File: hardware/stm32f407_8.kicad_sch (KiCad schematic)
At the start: 28 parts, among them J10 Conn_01x04, J8 USB_B_Mini, J9 Conn_01x04, SW3 SW TACT-SPST, U7 STM32F407VGT6, Y3 ABM8G-8.000MHZ-18-D2Y-T

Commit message: Complete Schematic for Power Section
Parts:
- renumbered C70 to C54, C66 to C55, C67 to C56, C62 to C57, C68 to C58, C63 to C59, C64 to C60, C71 to C61, C61 to C62, C65 to C63, C60 to C64, C59 to C65, C55 to C66, C56 to C67, C57 to C68, C58 to C69, C69 to C70, C72 to C71, R28 to R23, R23 to R25

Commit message: Organize schematic
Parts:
- J8: value USB_B_Mini -> GMSB0531112YEU
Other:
- note added: "C54 must be placed close to 1 VDD pin"
- note added: "Main Controller"
- note added: "Oscilator"
- note added: "UART & CAN"
- note added: "USB Mini B"
- note removed: "Must be placed close to 1 VDD pin"
- moved on the sheet: C54, C55, C56, C57, C58, C59, C60, C61, C62, C63, C64, C65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

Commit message: Link footprints to Symbols
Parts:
- C54, C55, C56, C57, C58, C59, C60, C61, C62, C63, C64, C65, C66, C67, C68, C69, C70, C71: footprint (none) -> STM32F407 Dev Kit Library:C_0805_2012Metric_Pad1.18x1.45mm_HandSolder
- FB4: footprint Package_DFN_QFN:QFN-16-1EP_4x4mm_P0.65mm_EP2.1x2.1mm -> STM32F407 Dev Kit Library:C_0805_2012Metric_Pad1.18x1.45mm_HandSolder
- J10, J9: footprint Package_QFP:LQFP-48_7x7mm_P0.5mm -> STM32F407 Dev Kit Library:PinHeader_1x04_P2.54mm_Vertical
- J8: footprint RF_Module:ST-SiP-LGA-86-11x7.3mm -> STM32F407 Dev Kit Library:USB_Mini-B_Wuerth_65100516121_Horizontal
- R23: footprint Package_QFP:LQFP-100_14x14mm_P0.5mm -> STM32F407 Dev Kit Library:R_0805_2012Metric_Pad1.20x1.40mm_HandSolder
- R24, R25: footprint (none) -> STM32F407 Dev Kit Library:R_0805_2012Metric_Pad1.20x1.40mm_HandSolder
- SW3: footprint Button_Switch_SMD:Nidec_Copal_CAS-120A -> STM32F407 Dev Kit Library:SW_Push_1P1T_NO_CK_KSC9xxG
- U7: footprint Package_QFP:LQFP-100_14x14mm_P0.5mm -> STM32F407 Dev Kit Library:LQFP-100_14x14mm_P0.5mm
- Y3: footprint (none) -> STM32F407 Dev Kit Library:Crystal_SMD_3225-4Pin_3.2x2.5mm_HandSoldering
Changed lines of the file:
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@@
 			)
 		)
-		(property "Footprint" "Package_QFP:LQFP-100_14x14mm_P0.5mm"
+		(property "Footprint" "STM32F407 Dev Kit Library:R_0805_2012Metric_Pad1.20x1.40mm_HandSolder"
 			(at 56.642 59.69 90)
 			(hide yes)
@@
 			)
 		)
-		(property "Footprint" ""
+		(property "Footprint" "STM32F407 Dev Kit Library:R_0805_2012Metric_Pad1.20x1.40mm_HandSolder"
 			(at 156.972 104.14 90)
 			(hide yes)
@@
 			)
 		)
-		(property "Footprint" ""
+		(property "Footprint" "STM32F407 Dev Kit Library:C_0805_2012Metric_Pad1.18x1.45mm_HandSolder"
 			(at 196.5452 156.21 0)
 			(hide yes)
@@
 			)
 		)
-		(property "Footprint" ""
+		(property "Footprint" "STM32F407 Dev Kit Library:C_0805_2012Metric_Pad1.18x1.45mm_HandSolder"
 			(at 166.0652 40.64 0)
 			(hide yes)
@@
 			)
 		)
-		(property "Footprint" "Package_QFP:LQFP-100_14x14mm_P0.5mm"
+		(property "Footprint" "STM32F407 Dev Kit Library:LQFP-100_14x14mm_P0.5mm"
 			(at 85.09 180.34 0)
 			(hide yes)
@@
 			)
 		)
-		(property "Footprint" ""
+		(property "Footprint" "STM32F407 Dev Kit Library:C_0805_2012Metric_Pad1.18x1.45mm_HandSolder"
 			(at 45.4152 63.5 0)
 			(hide yes)
@@
 			)
 		)
-		(property "Footprint" ""
+		(property "Footprint" "STM32F407 Dev Kit Library:C_0805_2012Metric_Pad1.18x1.45mm_HandSolder"
 			(at 143.2052 40.64 0)
 			(hide yes)
@@
 			)
 		)
-		(property "Footprint" ""
+		(property "Footprint" "STM32F407 Dev Kit Library:C_0805_2012Metric_Pad1.18x1.45mm_HandSolder"
 			(at 196.5452 128.27 0)
 			(hide yes)
@@
 			)
 		)
-		(property "Footprint" ""
+		(property "Footprint" "STM32F407 Dev Kit Library:C_0805_2012Metric_Pad1.18x1.45mm_HandSolder"
 			(at 78.4352 34.29 0)
 			(hide yes)
@@
 			)
 		)
-		(property "Footprint" ""
+		(property "Footprint" "STM32F407 Dev Kit Library:C_0805_2012Metric_Pad1.18x1.45mm_HandSolder"
 			(at 154.6352 40.64 0)
 			(hide yes)
@@
 			)
 		)
-		(property "Footprint" "Package_QFP:LQFP-48_7x7mm_P0.5mm"
+		(property "Footprint" "STM32F407 Dev Kit Library:PinHeader_1x04_P2.54mm_Vertical"
 			(at 229.87 116.84 0)
 			(hide yes)
@@
 			)
 		)
-		(property "Footprint" "RF_Module:ST-SiP-LGA-86-11x7.3mm"
+		(property "Footprint" "STM32F407 Dev Kit Library:USB_Mini-B_Wuerth_65100516121_Horizontal"
 			(at 213.36 76.2 0)
 			(hide yes)
@@
 			)
 		)
-		(property "Footprint" ""
+		(property "Footprint" "STM32F407 Dev Kit Library:C_0805_2012Metric_Pad1.18x1.45mm_HandSolder"
 			(at 55.5752 34.29 0)
 			(hide yes)
@@
 			)
 		)
-		(property "Footprint" "Package_QFP:LQFP-48_7x7mm_P0.5mm"
+		(property "Footprint" "STM32F407 Dev Kit Library:PinHeader_1x04_P2.54mm_Vertical"
 			(at 229.87 144.78 0)
 			(hide yes)
@@
 			)
 		)
-		(property "Footprint" ""
+		(property "Footprint" "STM32F407 Dev Kit Library:C_0805_2012Metric_Pad1.18x1.45mm_HandSolder"
 			(at 21.2852 34.29 0)
 			(hide yes)
@@
 			)
 		)
-		(property "Footprint" ""
+		(property "Footprint" "STM32F407 Dev Kit Library:Crystal_SMD_3225-4Pin_3.2x2.5mm_HandSoldering"
 			(at 210.82 35.56 0)
 			(hide yes)
@@
 			)
 		)
-		(property "Footprint" ""
+		(property "Footprint" "STM32F407 Dev Kit Library:C_0805_2012Metric_Pad1.18x1.45mm_HandSolder"
 			(at 89.8652 34.29 0)
 			(hide yes)
@@
 			)
 		)
-		(property "Footprint" ""
+		(property "Footprint" "STM32F407 Dev Kit Library:C_0805_2012Metric_Pad1.18x1.45mm_HandSolder"
 			(at 67.0052 34.29 0)
 			(hide yes)
@@
 			)
 		)
-		(property "Footprint" ""
+		(property "Footprint" "STM32F407 Dev Kit Library:C_0805_2012Metric_Pad1.18x1.45mm_HandSolder"
 			(at 207.01 39.6748 0)
 			(hide yes)
@@
 			)
 		)
-		(property "Footprint" ""
+		(property "Footprint" "STM32F407 Dev Kit Library:C_0805_2012Metric_Pad1.18x1.45mm_HandSolder"
 			(at 44.1452 34.29 0)
 			(hide yes)
@@
 			)
 		)
-		(property "Footprint" ""
+		(property "Footprint" "STM32F407 Dev Kit Library:R_0805_2012Metric_Pad1.20x1.40mm_HandSolder"
 			(at 149.352 104.14 90)
 			(hide yes)
@@
 			)
 		)
-		(property "Footprint" ""
+		(property "Footprint" "STM32F407 Dev Kit Library:C_0805_2012Metric_Pad1.18x1.45mm_HandSolder"
 			(at 131.7752 40.64 0)
 			(hide yes)
@@
 			)
 		)
-		(property "Footprint" ""
+		(property "Footprint" "STM32F407 Dev Kit Library:C_0805_2012Metric_Pad1.18x1.45mm_HandSolder"
 			(at 69.5452 170.18 0)
 			(hide yes)
@@
 			)
 		)
-		(property "Footprint" ""
+		(property "Footprint" "STM32F407 Dev Kit Library:C_0805_2012Metric_Pad1.18x1.45mm_HandSolder"
 			(at 32.7152 34.29 0)
 			(hide yes)
@@
 			)
 		)
-		(property "Footprint" "Package_DFN_QFN:QFN-16-1EP_4x4mm_P0.65mm_EP2.1x2.1mm"
+		(property "Footprint" "STM32F407 Dev Kit Library:C_0805_2012Metric_Pad1.18x1.45mm_HandSolder"
 			(at 118.618 27.94 90)
 			(hide yes)
@@
 			)
 		)
-		(property "Footprint" ""
+		(property "Footprint" "STM32F407 Dev Kit Library:C_0805_2012Metric_Pad1.18x1.45mm_HandSolder"
 			(at 58.1152 170.18 0)
 			(hide yes)
@@
 			)
 		)
-		(property "Footprint" "Button_Switch_SMD:Nidec_Copal_CAS-120A"
+		(property "Footprint" "STM32F407 Dev Kit Library:SW_Push_1P1T_NO_CK_KSC9xxG"
 			(at 29.21 60.96 0)
 			(hide yes)
@@
 			)
 		)
-		(property "Footprint" ""
+		(property "Footprint" "STM32F407 Dev Kit Library:C_0805_2012Metric_Pad1.18x1.45mm_HandSolder"
 			(at 207.01 29.5148 0)
 			(hide yes)

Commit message: Convert Schematic to PCB
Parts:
- removed SW3: SW TACT-SPST, STM32F407 Dev Kit Library:SW_Push_1P1T_NO_CK_KSC9xxG, symbol Switch:SW_MEC_5G
- removed Y3: ABM8G-8.000MHZ-18-D2Y-T, STM32F407 Dev Kit Library:Crystal_SMD_3225-4Pin_3.2x2.5mm_HandSoldering, symbol Device:Crystal
- added SW3: SW TACT-SPST, STM32F407 Dev Kit Library:SW_Push_SPST_NO_Alps_SKRK, symbol Switch:SW_Push
- added Y3: ABM8G-8.000MHZ-18-D2Y-T, STM32F407 Dev Kit Library:Crystal_SMD_3225-4Pin_3.2x2.5mm_HandSoldering, symbol Device:Crystal_GND24
- renumbered C57 to C55, C59 to C56, C58 to C57, C60 to C58, C61 to C59, C62 to C60, C63 to C61, C64 to C62, C65 to C63, C66 to C64, C67 to C65, C68 to C66, C69 to C67, C70 to C68, C71 to C69, C55 to C70, C56 to C71
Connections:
- net F407_NTRST: now also SW3.2
- net F407_OSC_IN: now also Y3.1
- net F407_OSC_OUT: now also Y3.3
- net GND: now also SW3.1, Y3.2 (G), Y3.4 (G)
- no-connect marks 2 -> 41

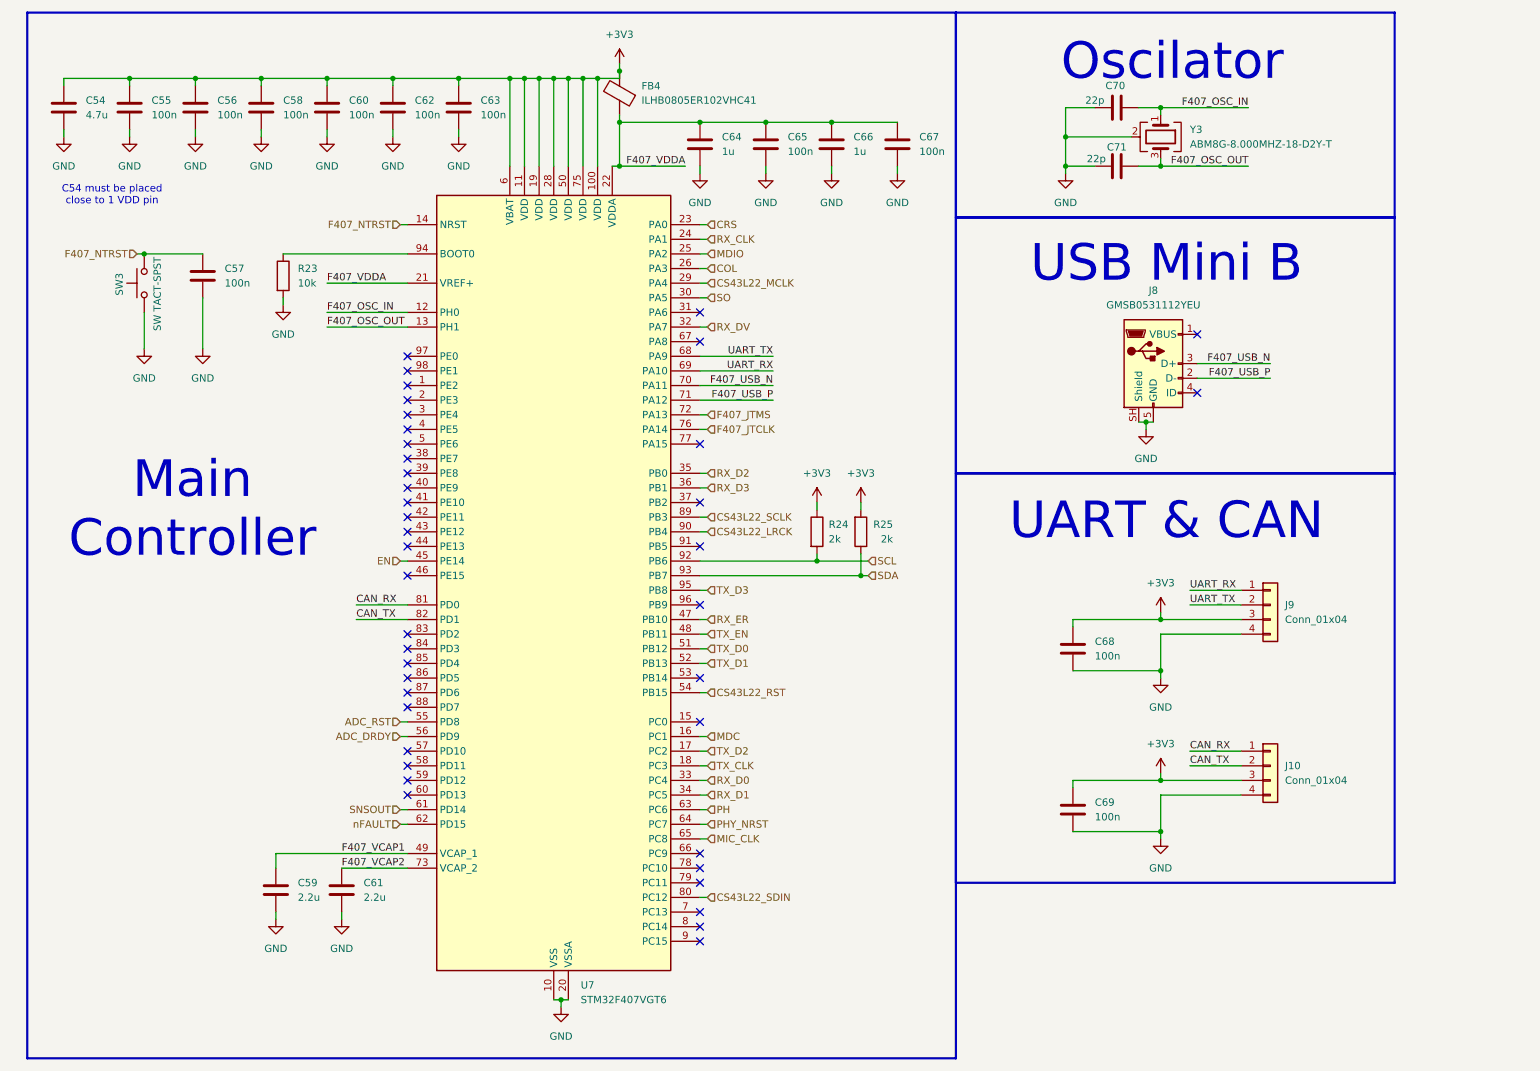
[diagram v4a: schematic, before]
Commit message: Route Ethernet section and add global labels
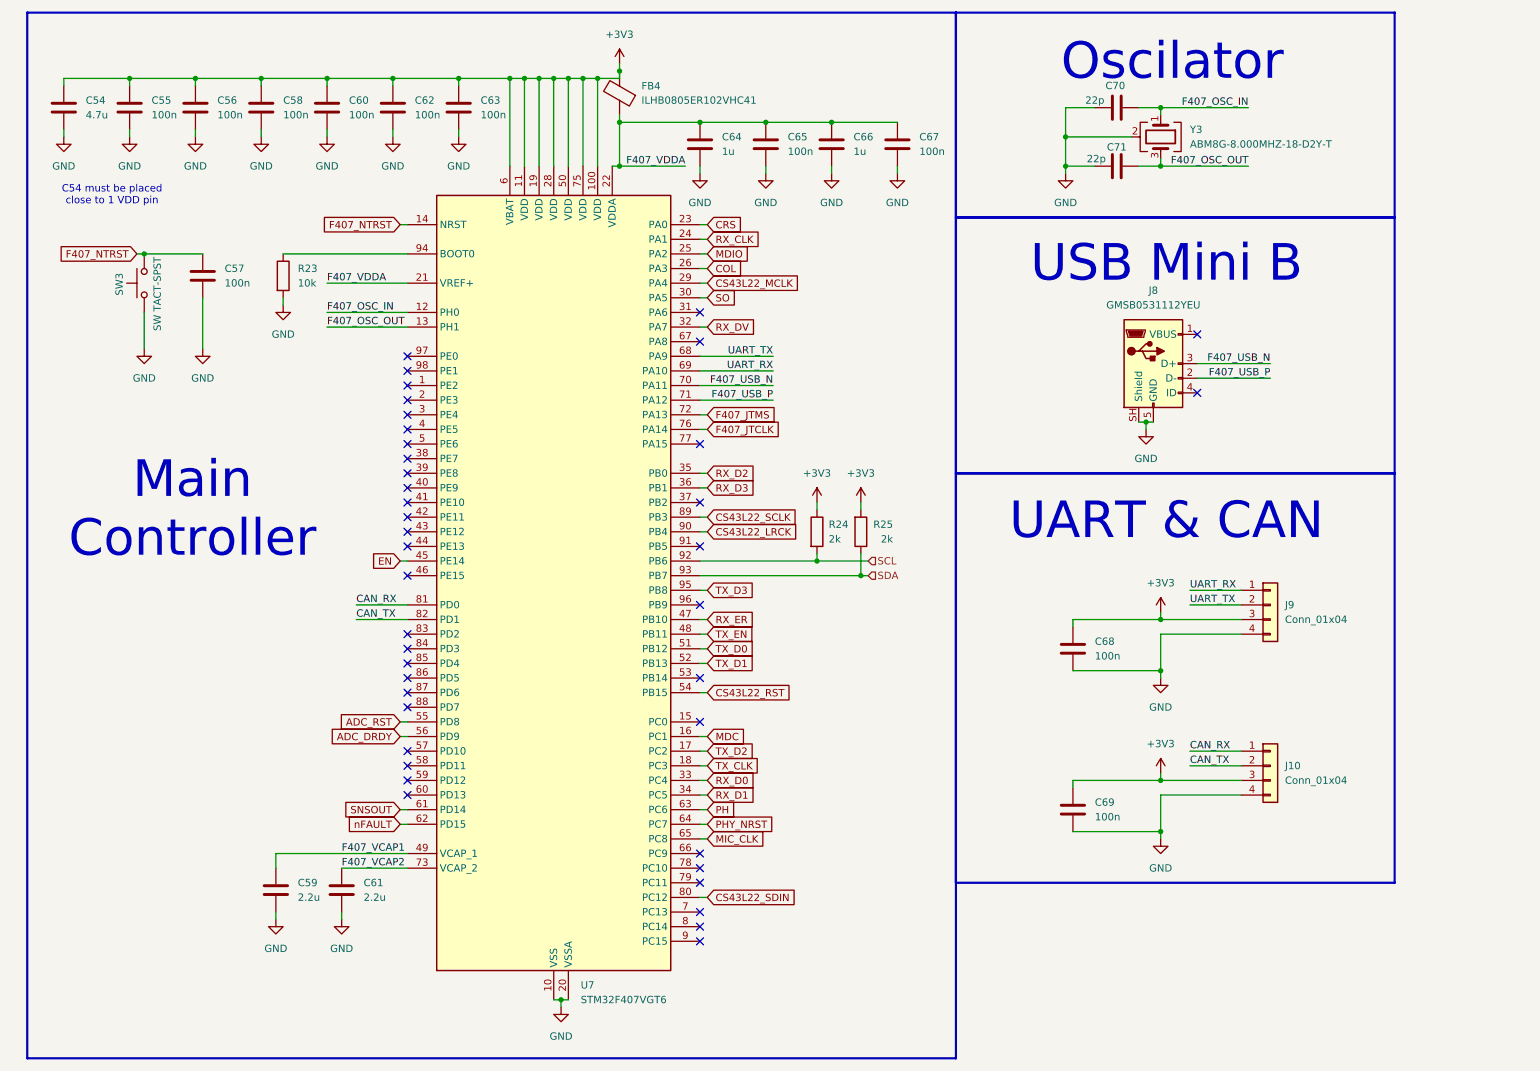
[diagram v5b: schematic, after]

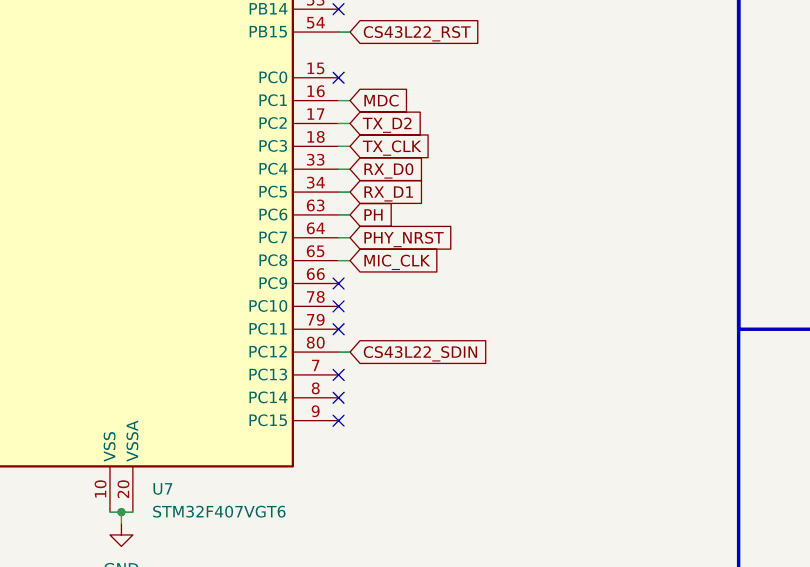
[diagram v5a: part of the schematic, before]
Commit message: Route Audio and ADC section
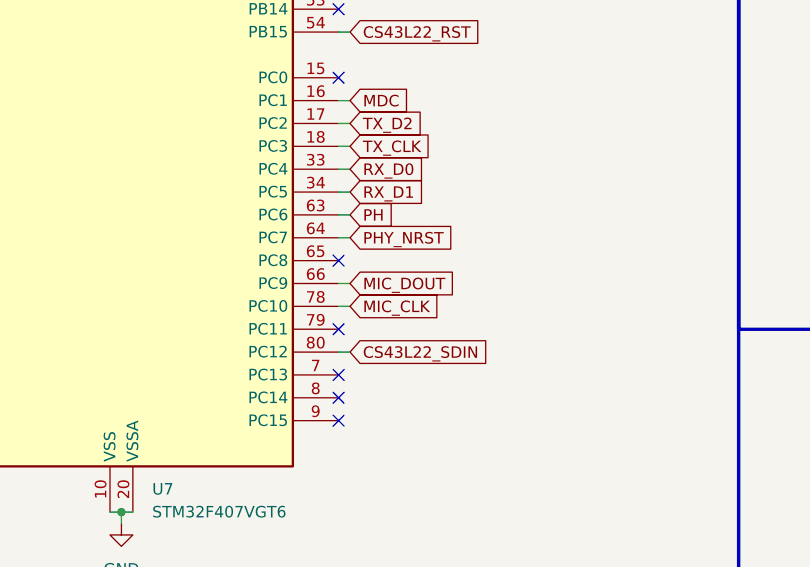
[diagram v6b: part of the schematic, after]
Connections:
- net MIC_CLK: now also U7.78 (PC10); no longer U7.65 (PC8)
- net MIC_DOUT: now reaches U7.66 (PC9)
- no-connect marks 41 -> 40

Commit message: Fix DRC errors
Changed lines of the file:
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@@
+		)
+	)
+	(global_label "SCL"
+		(shape input)
+		(at 160.02 109.22 0)
+		(fields_autoplaced yes)
+		(effects
+			(font
+				(size 1.27 1.27)
+			)
+			(justify left)
+		)
+		(property "Intersheetrefs" "${INTERSHEET_REFS}"
+			(at 166.5128 109.22 0)
+			(hide yes)
+			(show_name no)
+			(do_not_autoplace no)
+			(effects
+				(font
+					(size 1.27 1.27)
+				)
+				(justify left)
+			)
 		)
 	)
@@
 		)
 	)
+	(global_label "SDA"
+		(shape input)
+		(at 160.02 111.76 0)
+		(fields_autoplaced yes)
+		(effects
+			(font
+				(size 1.27 1.27)
+			)
+			(justify left)
+		)
+		(property "Intersheetrefs" "${INTERSHEET_REFS}"
+			(at 166.5733 111.76 0)
+			(hide yes)
+			(show_name no)
+			(do_not_autoplace no)
+			(effects
+				(font
+					(size 1.27 1.27)
+				)
+				(justify left)
+			)
+		)
+	)
 	(global_label "MIC_CLK"
 		(shape input)
@@
 		)
 	)
-	(hierarchical_label "SDA"
-		(shape input)
-		(at 160.02 111.76 0)
-		(effects
-			(font
-				(size 1.27 1.27)
-			)
-			(justify left)
-		)
-	)
-	(hierarchical_label "SCL"
-		(shape input)
-		(at 160.02 109.22 0)
-		(effects
-			(font
-				(size 1.27 1.27)
-			)
-			(justify left)
-		)
-	)
